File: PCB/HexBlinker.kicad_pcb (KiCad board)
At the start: 2 copper layers, 49.5 x 65.5 mm, 25 parts, among them J1 Conn_01x01_Socket, J3 USB_C_Receptacle_PowerOnly_6P, U1 4017, U2 NE555P

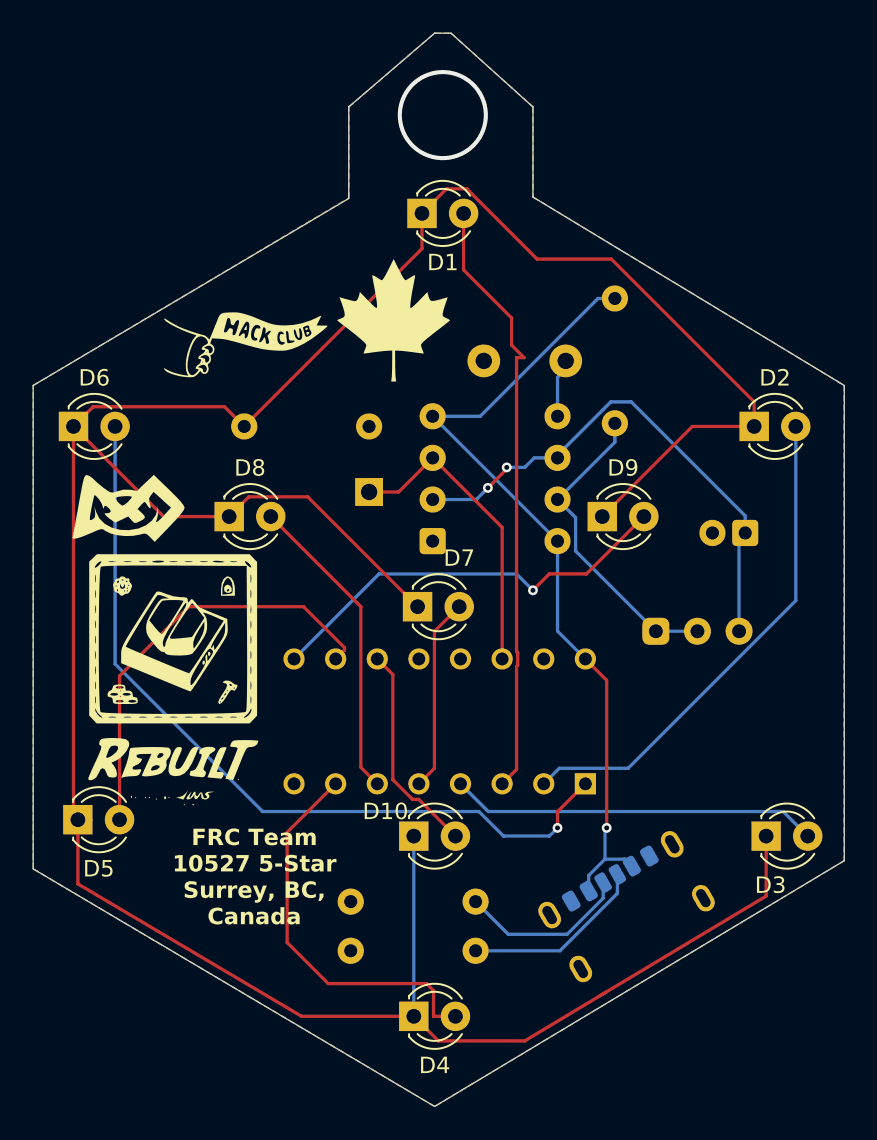
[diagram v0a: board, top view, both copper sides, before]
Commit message: Update to PCB before manufacturing.
I changed to pcb to reflect our new robot name and the Gracious Professionalism award we won at CANPAC 2026
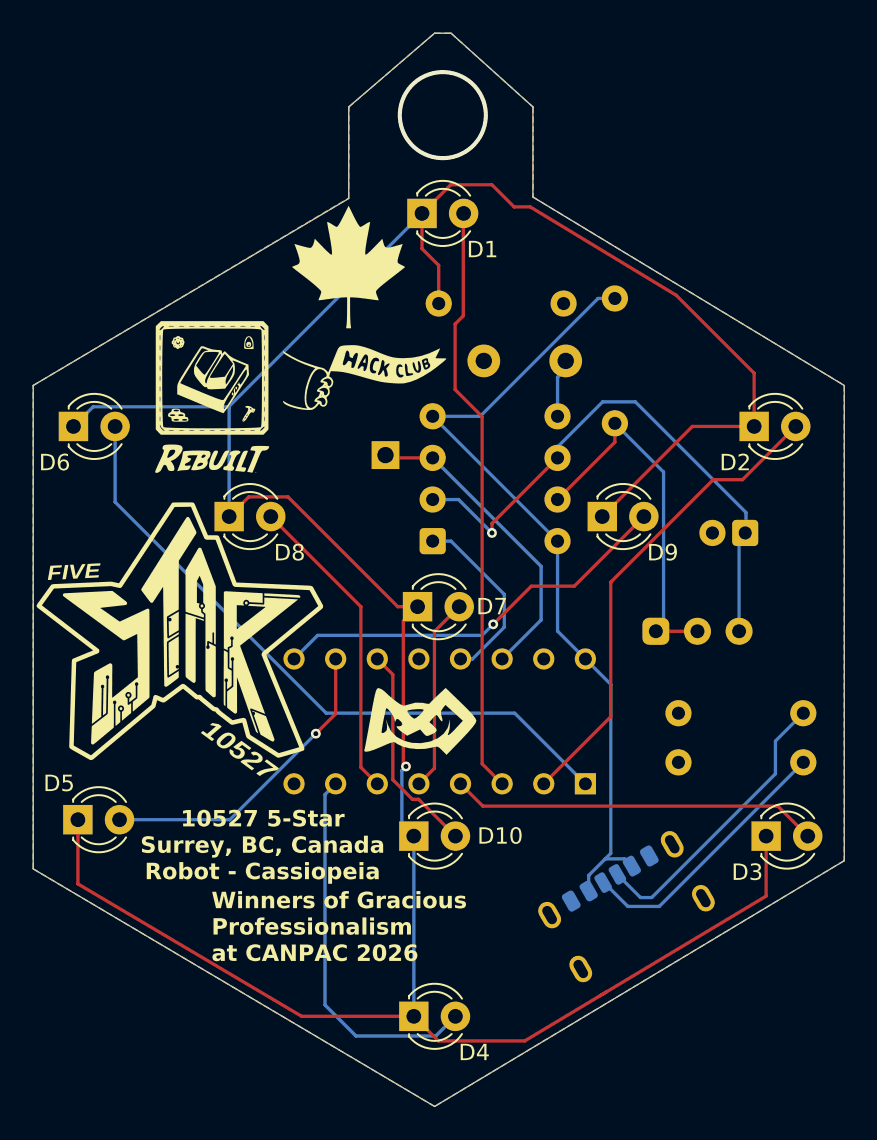
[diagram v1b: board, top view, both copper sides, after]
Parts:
- removed the G*** at (106.5, 95.0)
- added G***: LOGO, LOGO, F.Cu at (108.8, 77.2)
- added G***: LOGO, LOGO, F.Cu at (107.0, 92.5)
- added G***: LOGO, LOGO, B.Cu at (106.0, 96.0)
- moved R3 24.7 mm to (145.0, 97.0)
- moved G*** 22.0 mm to (127.2, 97.5)
- moved R4 21.7 mm to (145.0, 100.0)
- moved R1 14.0 mm to (122.8, 72.0)
- moved G*** 7.52 mm to (118.2, 76.5)
- moved G*** 4.26 mm to (117.2, 69.8)
- moved J1 2.46 mm to (119.5, 81.2)
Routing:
- net GND: track 0.00 -> 11.2 mm
- net Net-(D1-K): track 187.1 -> 176.9 mm, vias 0 -> 1
- net Net-(D6-A): track 49.5 -> 40.4 mm, vias 1 -> 0
- net Net-(D5-A): track 26.6 -> 19.2 mm, vias 0 -> 1
- net Net-(J3-CC1): track 11.3 -> 17.8 mm
- net Net-(J3-CC2): track 10.5 -> 16.5 mm
- net Net-(U2-DIS): track 19.2 -> 22.8 mm
- net TR: track 31.8 -> 34.2 mm, vias 2 -> 1
- net Net-(D2-A): track 30.6 -> 29.2 mm
- net Net-(D1-A): track 37.2 -> 36.2 mm
- net Net-(D4-A): track 24.0 -> 23.0 mm
- net Net-(D9-A): track 25.8 -> 24.9 mm
- net +5V: track 49.7 -> 49.9 mm, vias 1 -> 0
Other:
- board text added: "10527 5-Star Surrey, BC, Canada Robot - Cassiopeia"
- board text added: "2026 CANPAC Day 3 6:58:56 to 7:00:16"
- board text added: "By seeking support from neighboring teams and passing that along, they proved that teamwork is the brightest star in the constellation of success."
- board text added: "There is only one rating we could give them - Congratulations, Team number 10527 5-star Robotics"
- board text added: "This rising team set"
- board text added: "Winners of Gracious Professionalism at CANPAC 2026"
- board text added: "and their ambition even higher."
- board text added: "their goals sky-high"
- board text removed: "FRC Team 10527 5-Star Surrey, BC, Canada"
